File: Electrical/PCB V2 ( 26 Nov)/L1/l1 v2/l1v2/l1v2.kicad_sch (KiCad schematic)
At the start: 189 parts, among them J1 Conn_01x01_Socket, J2 Conn_01x01_Socket, SW1 SW_SPDT, U1 ESP32-WROOM-32D-N4, U2 CD74HC4067SM, U3 CD74HC4067SM

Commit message: unfinished ocb with parts list
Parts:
- removed U1: ESP32-WROOM-32D-N4, esp32 thinfy:MODULE_ESP32-WROOM-32D-N4, symbol ESP32:ESP32-WROOM-32D-N4
- added U1: 102010428, RF_Module:MCU_Seeed_ESP32C3, symbol xiao_seed:102010428
- H1, H10, H11, H12, H13, H14, H15, H16, H17, H18, H19, H2, H20, H21, H3, H4, H5, H6, H7, H8, H9: footprint MountingHole:MountingHole_3.2mm_M3 -> MountingHole:MountingHole_3.2mm_M3_DIN965_Pad
- LED1, LED10, LED11, LED12, LED13, LED14, LED15, LED16, LED17, LED18, LED19, LED2, LED20, LED21, LED22, LED23, LED24, LED25, LED26, LED27, LED28, LED29, LED3, LED30, LED31, LED32, LED4, LED5, LED6, LED7, LED8, LED9: footprint LED_SMD:LED_0201_0603Metric -> LED_SMD:LED_PLCC_2835
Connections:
- net 3v3: now also U1.12 (3V3)
- net GND: now also LED1.1 (K), LED10.1 (K), LED11.1 (K), LED12.1 (K), LED13.1 (K), LED14.1 (K), LED15.1 (K), LED16.1 (K), LED17.1 (K), LED18.1 (K), LED19.1 (K), LED2.1 (K), LED20.1 (K), LED21.1 (K), LED22.1 (K), LED23.1 (K), LED24.1 (K), LED25.1 (K), LED26.1 (K), LED27.1 (K), LED28.1 (K), LED29.1 (K), LED3.1 (K), LED30.1 (K), LED31.1 (K), LED32.1 (K), LED4.1 (K), LED5.1 (K), LED6.1 (K), LED7.1 (K), LED8.1 (K), LED9.1 (K), TP2.1, U1.13 (GND)
- net GNDPWR: no longer LED1.1 (K), LED10.1 (K), LED11.1 (K), LED12.1 (K), LED13.1 (K), LED14.1 (K), LED15.1 (K), LED16.1 (K), LED17.1 (K), LED18.1 (K), LED19.1 (K), LED2.1 (K), LED20.1 (K), LED21.1 (K), LED22.1 (K), LED23.1 (K), LED24.1 (K), LED25.1 (K), LED26.1 (K), LED27.1 (K), LED28.1 (K), LED29.1 (K), LED3.1 (K), LED30.1 (K), LED31.1 (K), LED32.1 (K), LED4.1 (K), LED5.1 (K), LED6.1 (K), LED7.1 (K), LED8.1 (K), LED9.1 (K), TP2.1
- net at LED_1.1, LED_10.1, LED_11.1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: no longer LED_17.1, LED_18.1, LED_19.1, LED_20.1, LED_21.1, LED_22.1, LED_23.1, LED_24.1, LED_25.1, LED_26.1, LED_27.1, LED_28.1, LED_29.1, LED_30.1, LED_31.1, LED_32.1
- net at U3.1 (COM): no longer U2.1 (COM)
- new net: LED_17.1, LED_18.1, LED_19.1, LED_20.1, LED_21.1, LED_22.1, LED_23.1, LED_24.1, LED_25.1, LED_26.1, LED_27.1, LED_28.1, LED_29.1, LED_30.1, LED_31.1, LED_32.1
- no-connect marks 25 -> 15
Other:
- moved on the sheet: LED_18, LED_19, LED_20, LED_21, LED_22, LED_23, LED_24, LED_25, LED_26, LED_27, LED_28, LED_29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

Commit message: hahaha
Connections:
- net 3v3: now also LED_1.1, LED_10.1, LED_11.1, LED_12.1, LED_13.1, LED_14.1, LED_15.1, LED_16.1, LED_17.1, LED_18.1, LED_19.1, LED_2.1, LED_20.1, LED_21.1, LED_22.1, LED_23.1, LED_24.1, LED_25.1, LED_26.1, LED_27.1, LED_28.1, LED_29.1, LED_3.1, LED_30.1, LED_31.1, LED_32.1, LED_4.1, LED_5.1, LED_6.1, LED_7.1, LED_8.1, LED_9.1

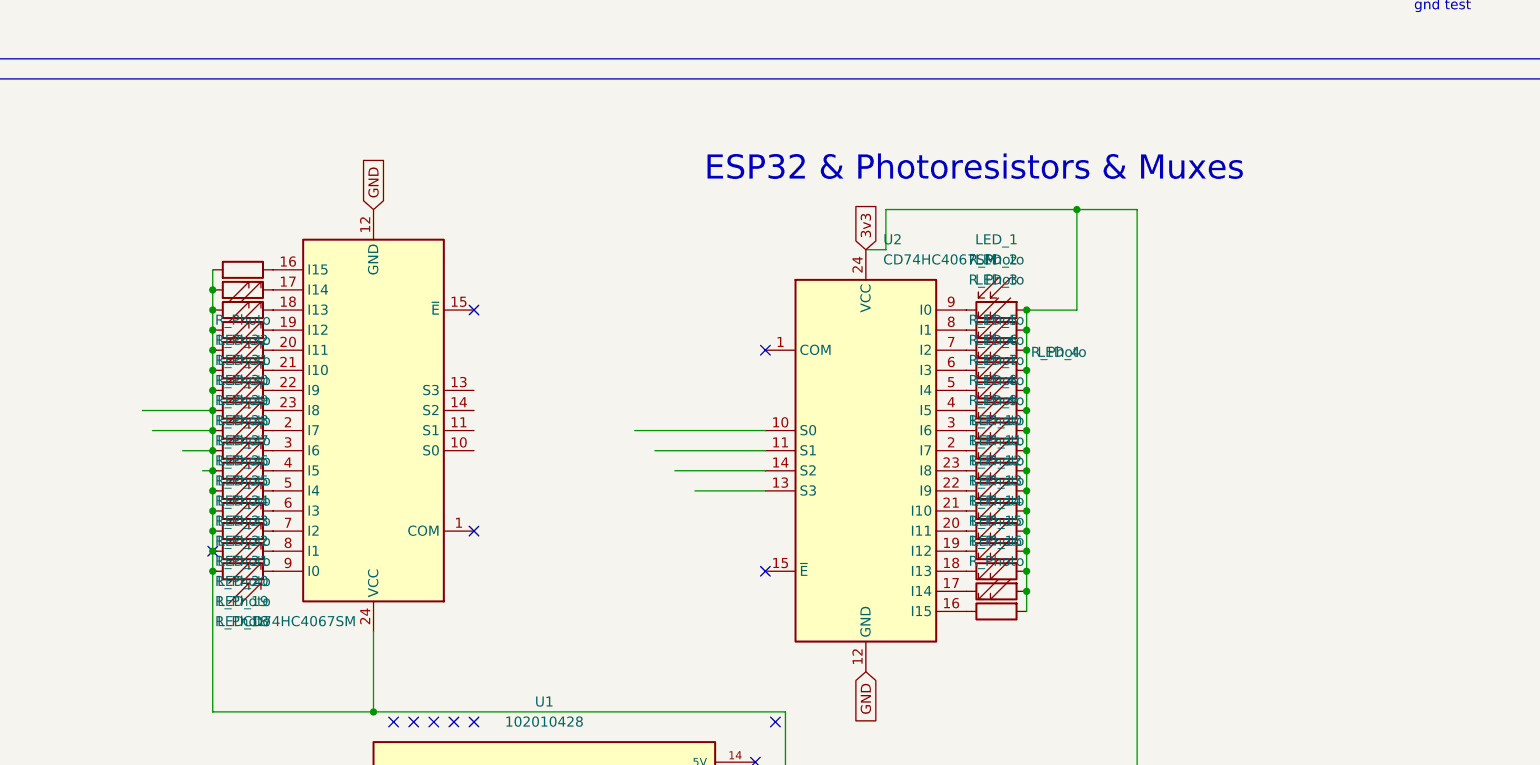
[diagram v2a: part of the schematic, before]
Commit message: wireed photoresistors for l1
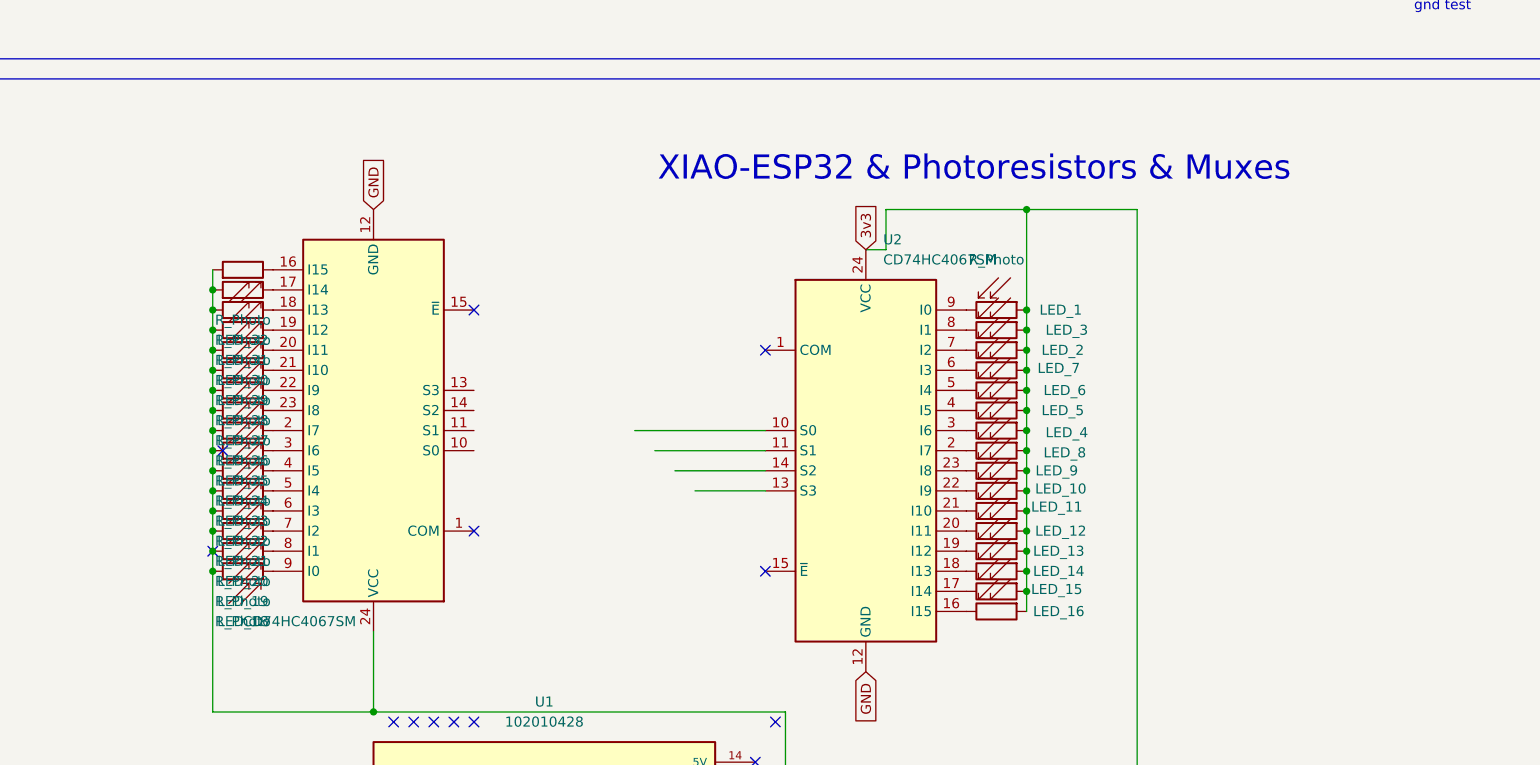
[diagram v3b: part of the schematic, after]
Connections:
- net at LED_7.2: now also U2.6 (I3); no longer U2.3 (I6)
- net at LED_4.2: now also U2.3 (I6); no longer U2.6 (I3)
- net at LED_6.2: now also U2.5 (I4); no longer U2.4 (I5)
- net at LED_3.2: now also U2.8 (I1); no longer U2.7 (I2)
- net at LED_2.2: now also U2.7 (I2); no longer U2.8 (I1)
- net at LED_5.2: now also U2.4 (I5); no longer U2.5 (I4)
- no-connect marks 15 -> 16
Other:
- note added: "XIAO-ESP32 & Photoresistors & Muxes"
- note removed: "ESP32 & Photoresistors & Muxes"
- moved on the sheet: LED_2, LED_3, LED_4, LED_5, LED_6, LED_7

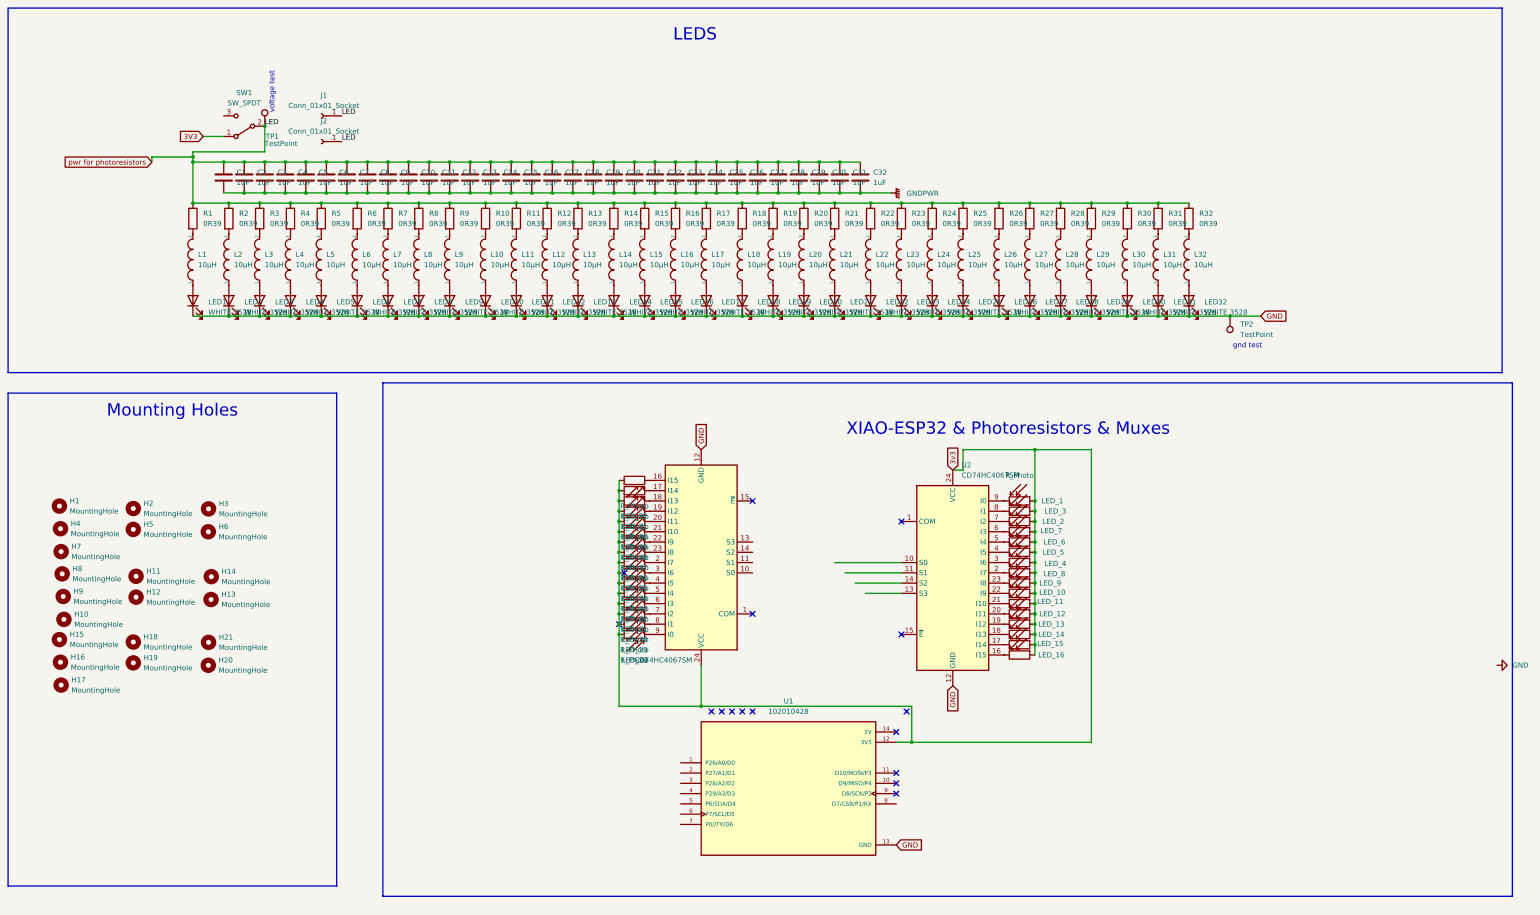
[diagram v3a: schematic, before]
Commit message: did led wiring to 3v3 and to muxes.
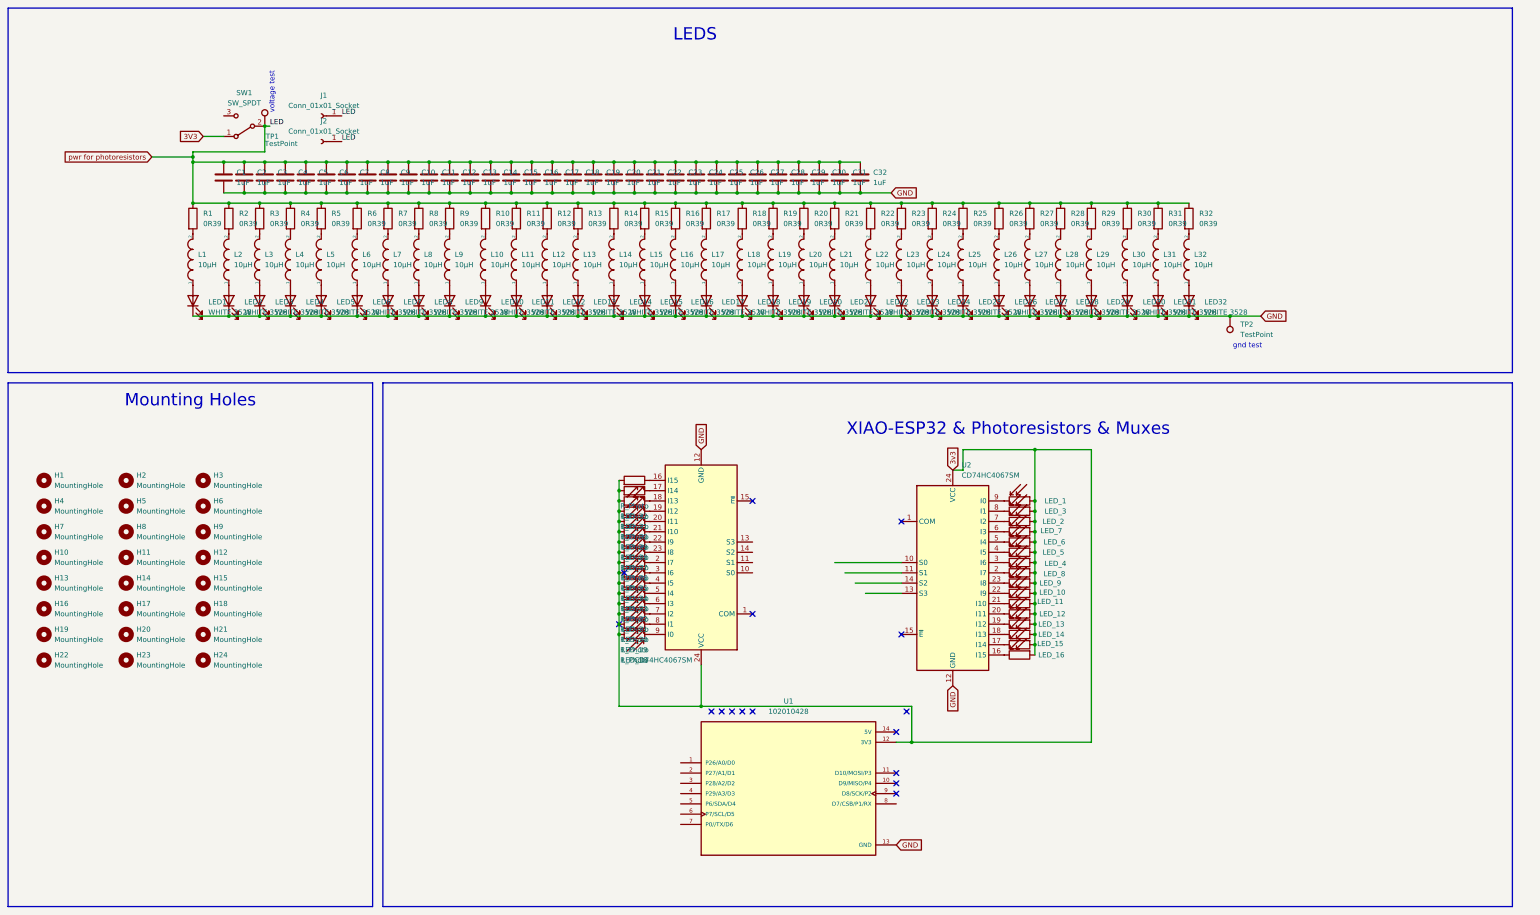
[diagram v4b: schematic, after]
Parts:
- added H22, H23, H24: MountingHole, MountingHole:MountingHole_3.2mm_M3_DIN965_Pad, symbol Mechanical:MountingHole
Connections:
- net GNDPWR is gone; now on net GND: C1.2, C10.2, C11.2, C12.2, C13.2, C14.2, C15.2, C16.2, C17.2, C18.2, C19.2, C2.2, C20.2, C21.2, C22.2, C23.2, C24.2, C25.2, C26.2, C27.2, C28.2, C29.2, C3.2, C30.2, C31.2, C32.2, C4.2, C5.2, C6.2, C7.2, C8.2, C9.2
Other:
- moved on the sheet: H1, H10, H11, H12, H13, H14, H15, H16, H17, H18, H19, H2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

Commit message: added l2 dxf, did some more stuff to l1
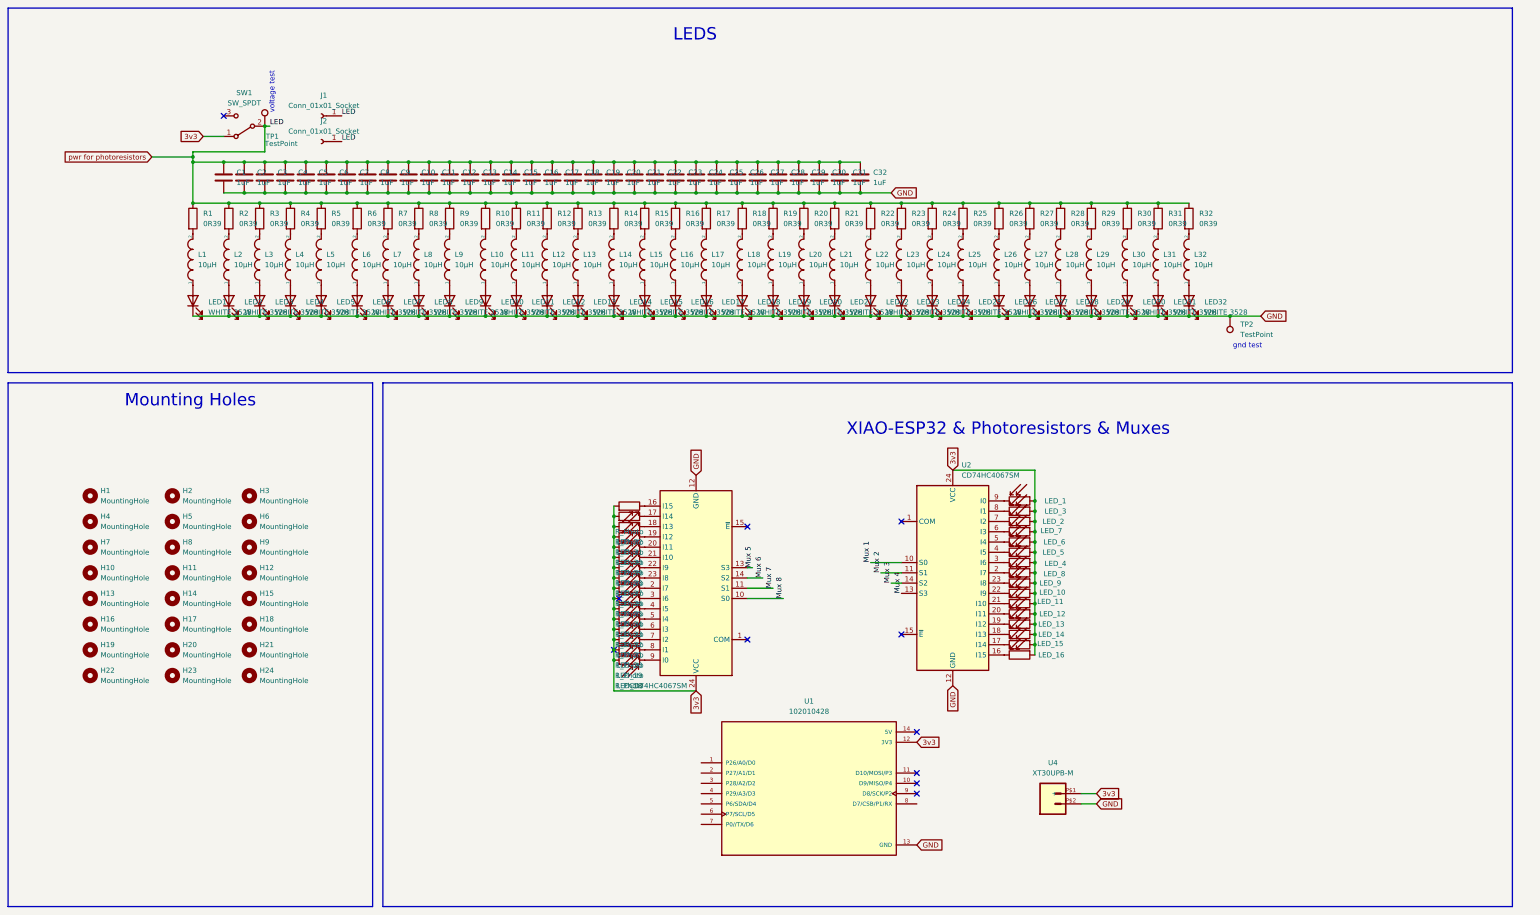
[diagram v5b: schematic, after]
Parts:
- added U4: XT30UPB-M, xt30-m:XT30UPB-M, symbol XT30UPB-M:XT30UPB-M
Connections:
- net 3V3 is gone; now on net 3v3: SW1.1 (A)
- net 3v3: now also U4.P$1 (+)
- net GND: now also U4.P$2 (-)
- net Mux 8: now reaches U3.10 (S0)
- net Mux 7: now reaches U3.11 (S1)
- net Mux 5: now reaches U3.13 (S3)
- net Mux 6: now reaches U3.14 (S2)
- net Mux 1 : now reaches U2.10 (S0)
- net Mux 2: now reaches U2.11 (S1)
- net Mux 4: now reaches U2.13 (S3)
- net Mux 3: now reaches U2.14 (S2)
- no-connect marks 16 -> 11
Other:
- moved on the sheet: H1, H10, H11, H12, H13, H14, H15, H16, H17, H18, H19, H2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
